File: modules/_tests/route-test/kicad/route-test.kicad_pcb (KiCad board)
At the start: 2 copper layers, 40 x 32 mm, 8 parts, among them J1 LEFT, J2 RIGHT

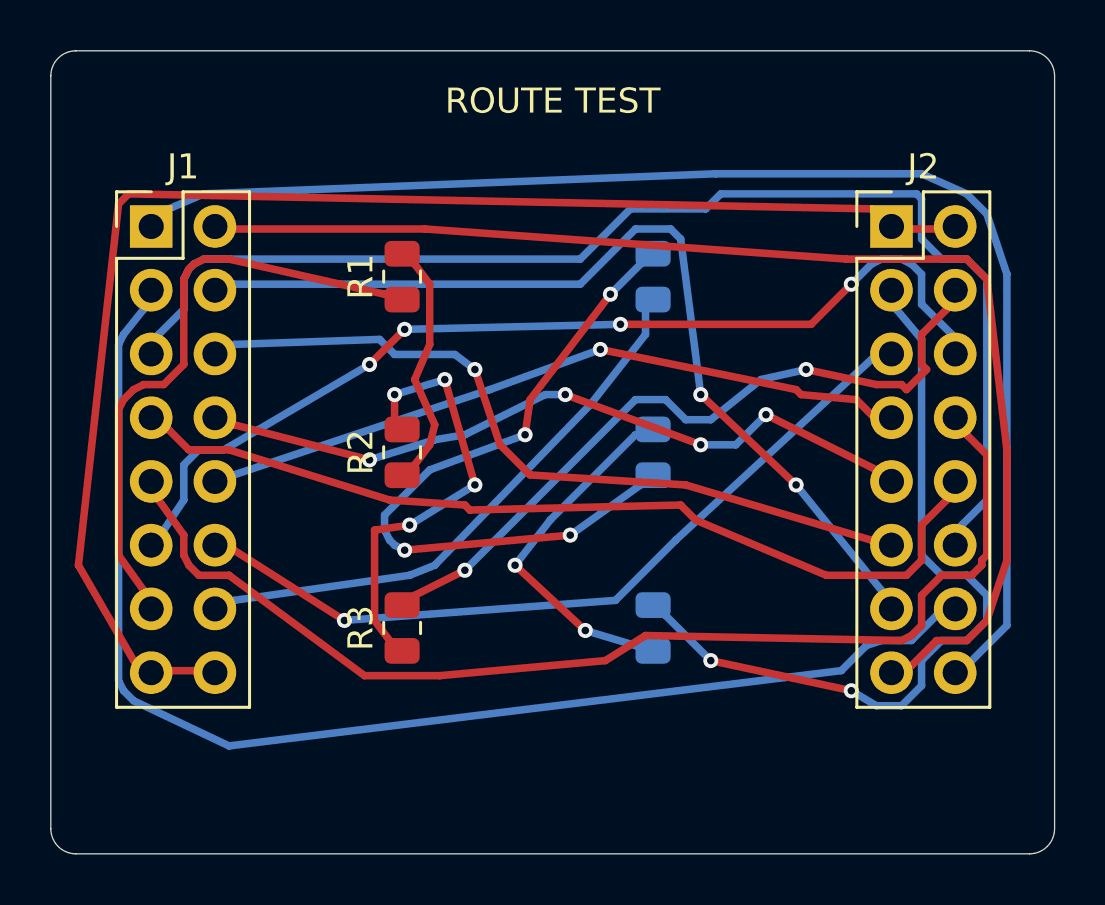
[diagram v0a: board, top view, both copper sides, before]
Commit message: Router: charge history congestion in the same currency as present congestion
Chasing the via-count gap Freerouting exposed found a defect in our
implementation of negotiated congestion, not a mistuned via cost.

Present congestion grew as 1.4^round while history congestion accumulated a
flat +1 per round, so by round 200 the present term was about 1e29 and history
at most 200. History was arithmetically irrelevant, the negotiation had no
memory, and two nets in conflict simply traded places forever. McMurchie &
Ebeling's convergence argument needs a cell that has been fought over to stay
expensive after it falls free.

Found by sweeping the via cost from 10 to 320 over every benchmark board:
legality flipped on and off as the cost moved (reversal legal at 25 and 40,
illegal at 15, 30 and 320), and ten times the negotiation budget fixed
neither failing cost. A stall, not slow convergence.

History is now charged +pres per round. The exponent is capped at 500 because
1.4^2100 overflows a Double to infinity, which would poison every cost in the
penalty array.

Results:
- the sweep goes from 11 of 17 legal to 24 of 24; every via cost from 10 to
  320 converges on every board
- route-test at the unchanged default via cost: 27 vias and 717.67 mm become 7
  vias and 698.69 mm, against Freerouting's 6 vias and 690.79 mm, so the via
  gap closes from 4.5x to 1.17x and the copper gap from 3.9% to 1.1%
- the one remaining reversal failure now responds to budget, which is what the
  algorithm promises and previously did not; the default budget goes from 200
  to 600, and since the loop exits as soon as nothing is contested, boards that
  settle early pay nothing for it

The via cost stays at 40. After the fix no value is undominated everywhere:
40 gives the fewest vias on route-test and is beaten on both axes by 25 and 30
on the attenuverter and on reversal, while 20 wins route-test and then spends
51 vias on reversal where 25 spends 9. Too wide a spread to tune against five
bo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
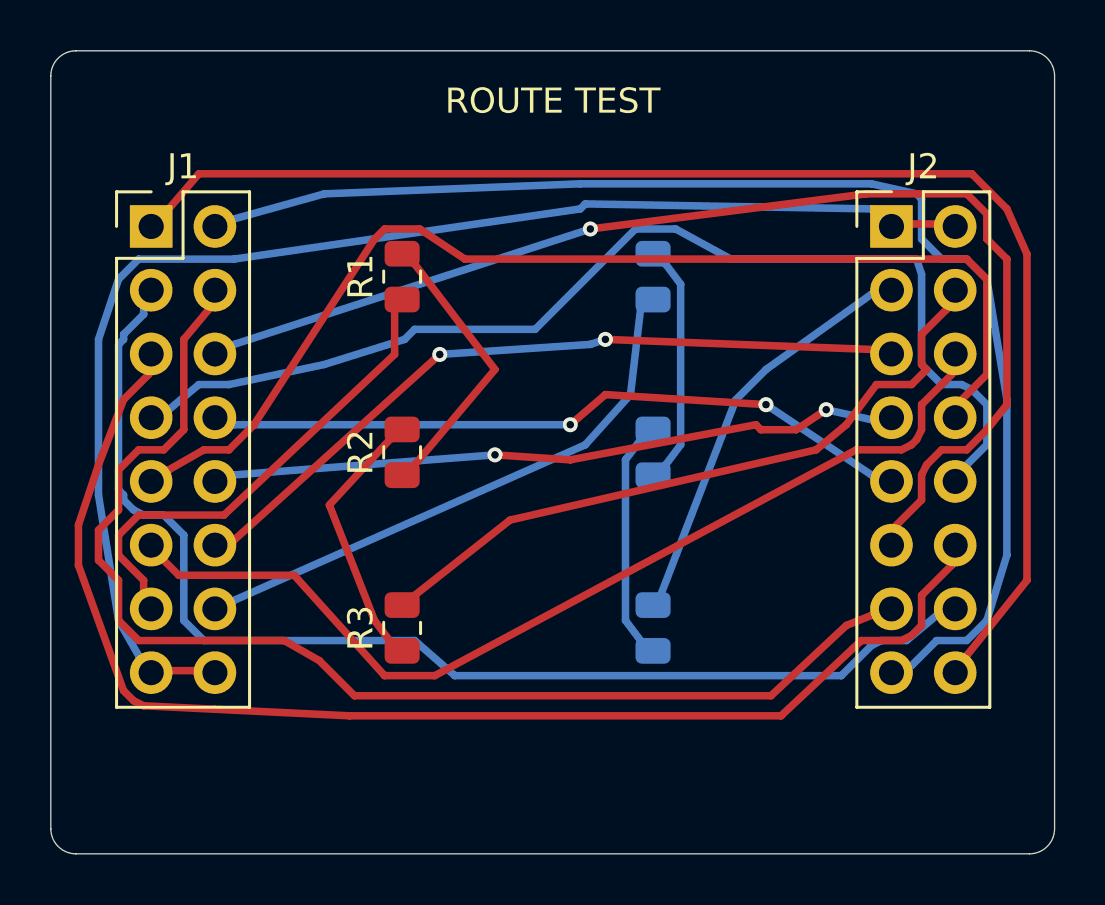
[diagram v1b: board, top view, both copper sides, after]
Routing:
- net /RF: track 28.1 -> 9.70 mm, vias 4 -> 0
- net /X6: track 30.5 -> 47.9 mm
- net /RH: track 31.7 -> 16.5 mm, vias 2 -> 0
- net /X4: track 37.4 -> 49.0 mm, vias 2 -> 0
- net /X7: track 36.1 -> 44.3 mm
- net /RC: track 17.7 -> 10.8 mm, vias 4 -> 0
- net /RA: track 24.4 -> 19.6 mm
- net /RG: track 14.5 -> 9.70 mm, vias 2 -> 0
- net /X3: track 51.2 -> 47.8 mm
- net GND: track 56.1 -> 53.0 mm
- net /X2: track 49.5 -> 51.7 mm
- net /X12: track 31.7 -> 29.9 mm, vias 1 -> 2
- net /RD: track 29.2 -> 27.5 mm, vias 2 -> 0
- net /X1: track 53.6 -> 55.2 mm
- net /RB: track 10.0 -> 11.5 mm
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
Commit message: Net order dominates the router; measure what analog layout actually binds
Two threads, both driven by measurement rather than by assumption.

## The router: ordering beats every other setting

The via-cost spread left over from the last session was path dependence, not
noise. The negotiation only reroutes nets that are in conflict, so a net that
took a wasteful path in round one and was never contested again keeps it to
the end, and final quality follows the order conflicts happened to appear in.

Two changes. A post-convergence descent (rcImproveRounds) offers every net one
more route against the others' finished copper and keeps it only when it is
cheaper by the measure the A* itself minimises, so total cost strictly
decreases and it terminates. And multi-start (rcStarts): the negotiation runs
once per net ordering and the best result is kept, lexicographically on faults,
then contested cells, then cost, never a weighted sum. The orderings are four
named heuristics -- most terminals first, fewest first, longest span first,
shortest first -- and then deterministic shuffles; hardest-first against
easiest-first is a real disagreement in the literature and neither wins on
every board, which is the argument for running both.

Measured at the default via cost over the three congested boards:

  starts | reversal            | route-test | attenuverter
  1      | illegal, 202 vias   | 30 vias    | 9 vias
  2      | illegal             | 17 vias    | 7 vias
  4      | 23 vias             |  9 vias    | 5 vias
  6      | 14 vias             |  9 vias    | 5 vias
  8      | identical to 6      | identical  | identical

A single ordering leaves the crossing fixture illegal with 202 vias; six get
it to 14. Nothing else in the router buys a factor of fourteen, and the curve
is flat past six. The descent is separately worth one or two vias, and needed
its conflict test fixed: contest is symmetric, and checking only "my new
copper in someone else's halo" accepted reroutes that sw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
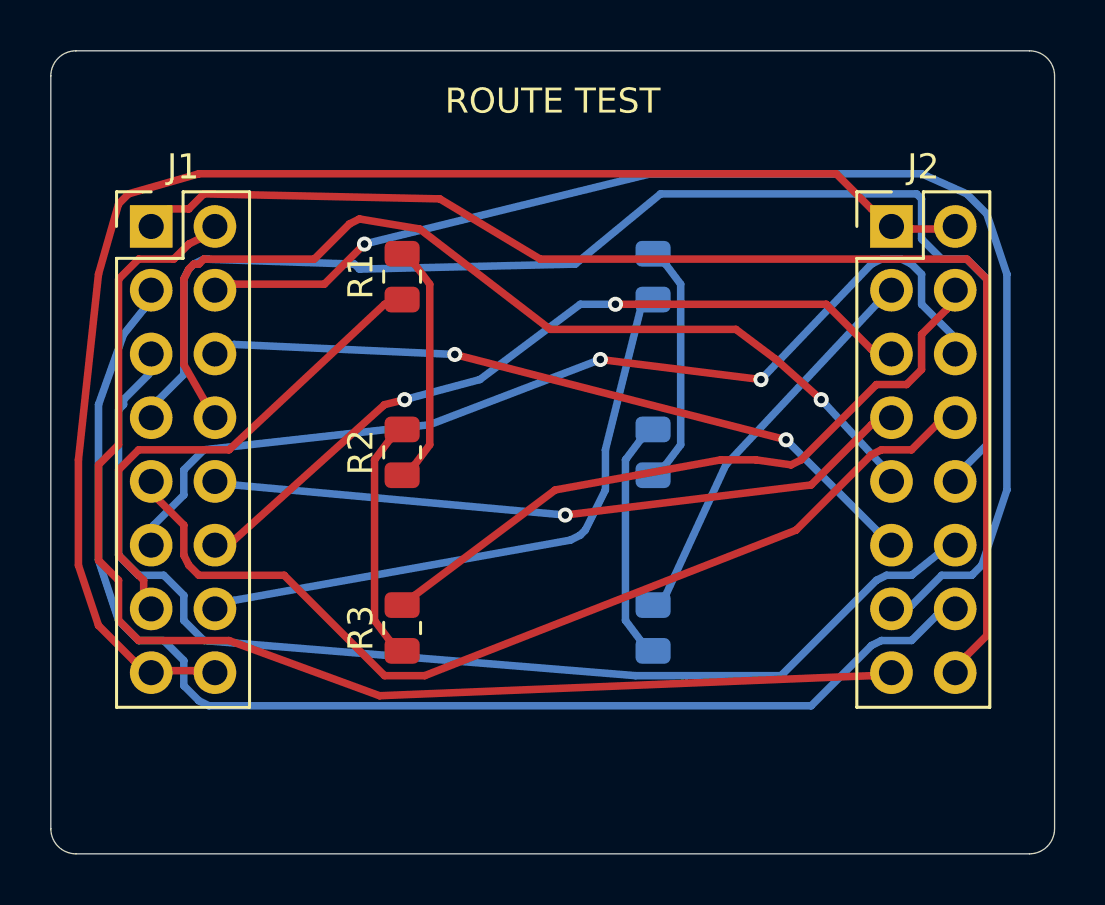
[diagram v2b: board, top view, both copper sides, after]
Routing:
- net /X6: track 47.9 -> 29.2 mm, vias 1 -> 2
- net /X8: track 28.4 -> 39.0 mm, vias 2 -> 1
- net /X7: track 44.3 -> 50.3 mm
- net /X9: track 44.9 -> 39.1 mm
- net /X5: track 51.6 -> 45.9 mm
- net /X1: track 55.2 -> 51.0 mm
- net GND: track 53.0 -> 56.9 mm
- net /X3: track 47.8 -> 50.6 mm
- net /RE: track 22.9 -> 25.0 mm
- net /RB: track 11.5 -> 9.70 mm
- net /X4: track 49.0 -> 50.9 mm, vias 0 -> 1
- net /X2: track 51.7 -> 50.4 mm
- net /RC: track 10.8 -> 9.70 mm
- net /X12: track 29.9 -> 31.0 mm
- net /X10: track 27.5 -> 28.1 mm, vias 2 -> 1
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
